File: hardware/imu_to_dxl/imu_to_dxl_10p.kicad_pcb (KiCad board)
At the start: 2 copper layers, 141.9 x 72.9 mm, 897 parts, among them CN1 B3B-EH-A (LF)(SN), CN2 B3B-PH-K-S(LF)(SN), J1 1.8mm螺丝孔, J2 1.8mm螺丝孔, J3 1.8mm螺丝孔, J4 1.8mm螺丝孔, Q1 MMBT3906, U1 ETA2845S2G_C22362741, U2 GD32F303CCT6, U3 LSM6DSV16XTR, U4 SN74LVC1G126DBVR, U5 SN74LVC1G125DBV, U6 ME6211C18M5G-N, X1 XL2EL89CSI-111YLC-12M

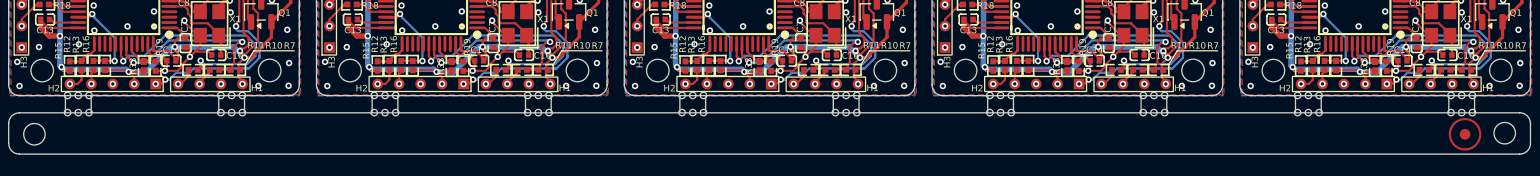
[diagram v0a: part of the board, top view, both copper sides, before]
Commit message: 修改IMU工作电压到5V；拼板文件优化
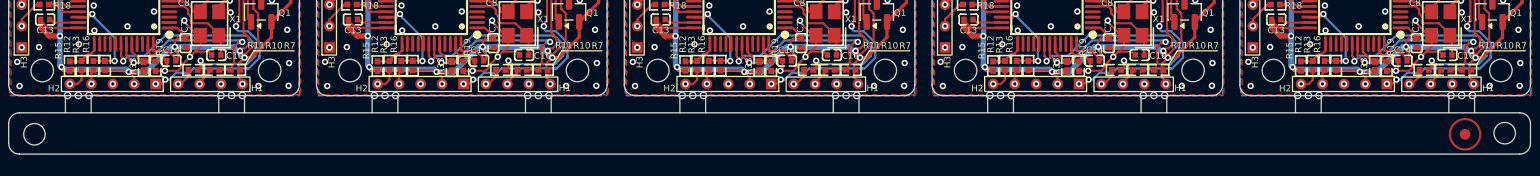
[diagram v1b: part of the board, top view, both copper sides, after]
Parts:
- removed the REF** at (72.4, 167.0)
- removed the REF** at (101.0, 167.0)
- removed the REF** at (87.7, 167.0)
- removed the REF** at (115.4, 167.0)
- removed the REF** at (73.4, 167.0)
- removed the REF** at (159.4, 167.0)
- removed the REF** at (86.7, 167.0)
- removed the REF** at (172.8, 167.0)
- removed the REF** at (60.1, 167.0)
- removed the REF** at (146.1, 167.0)
- removed the REF** at (88.7, 167.0)
- removed the REF** at (188.1, 167.0)
- removed the REF** at (174.8, 167.0)
- removed the REF** at (158.4, 167.0)
- removed the REF** at (103.0, 167.0)
- removed the REF** at (102.0, 167.0)
- removed the REF** at (74.4, 167.0)
- removed the REF** at (144.1, 167.0)
- removed the REF** at (173.8, 167.0)
- removed the REF** at (130.7, 167.0)
- removed the REF** at (59.1, 167.0)
- removed the REF** at (145.1, 167.0)
- removed the REF** at (117.4, 167.0)
- removed the REF** at (131.7, 167.0)
- removed the REF** at (160.4, 167.0)
- removed the REF** at (58.1, 167.0)
- removed the REF** at (116.4, 167.0)
- removed the REF** at (187.1, 167.0)
- removed the REF** at (129.7, 167.0)
- removed the REF** at (189.1, 167.0)
